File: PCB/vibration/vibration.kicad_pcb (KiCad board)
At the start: 2 copper layers, 45 x 65 mm, 21 parts, among them J1 Conn_01x02, J2 Conn_01x03, J3 Conn_01x03, J4 Conn_01x04, J5 Conn_01x04, Q1 BSS138, Q2 BSS138, U1 NRF24L01_Breakout

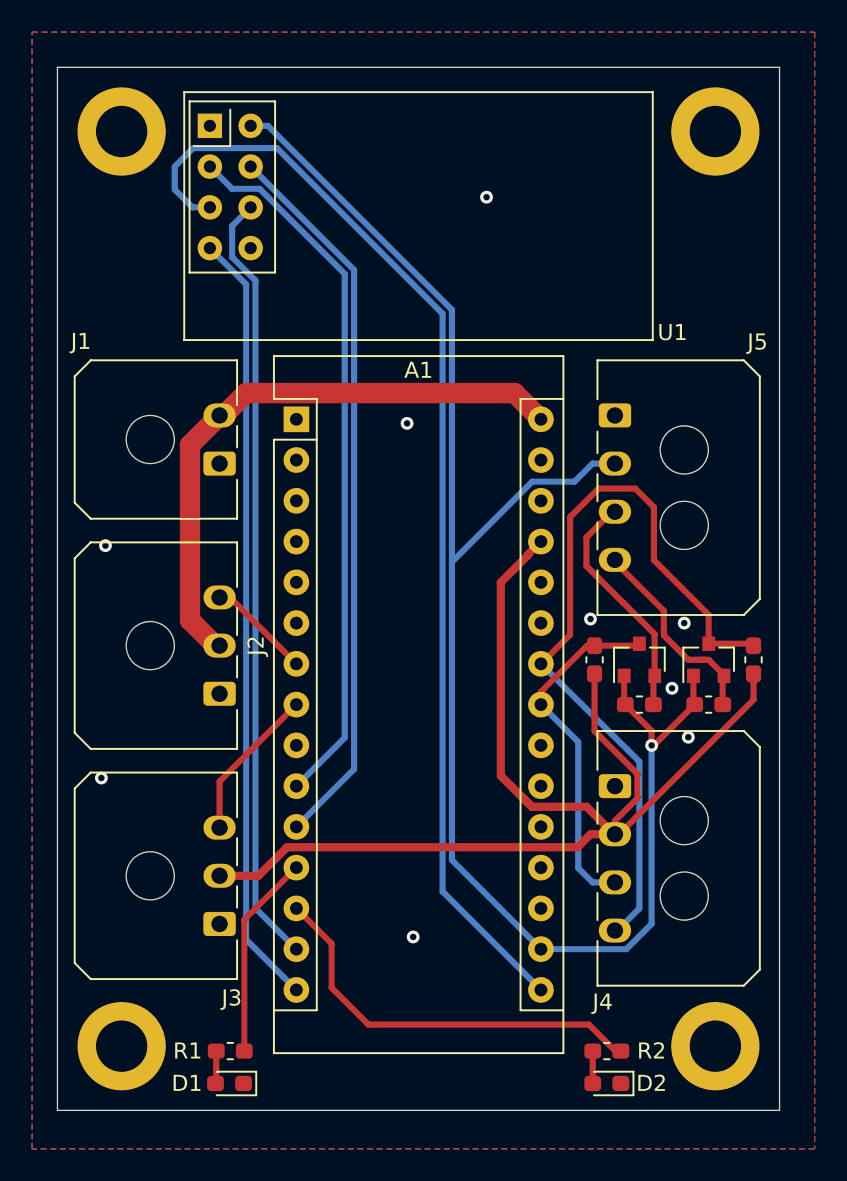
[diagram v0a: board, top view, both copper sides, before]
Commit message: Vibration review complete. Create gerbers
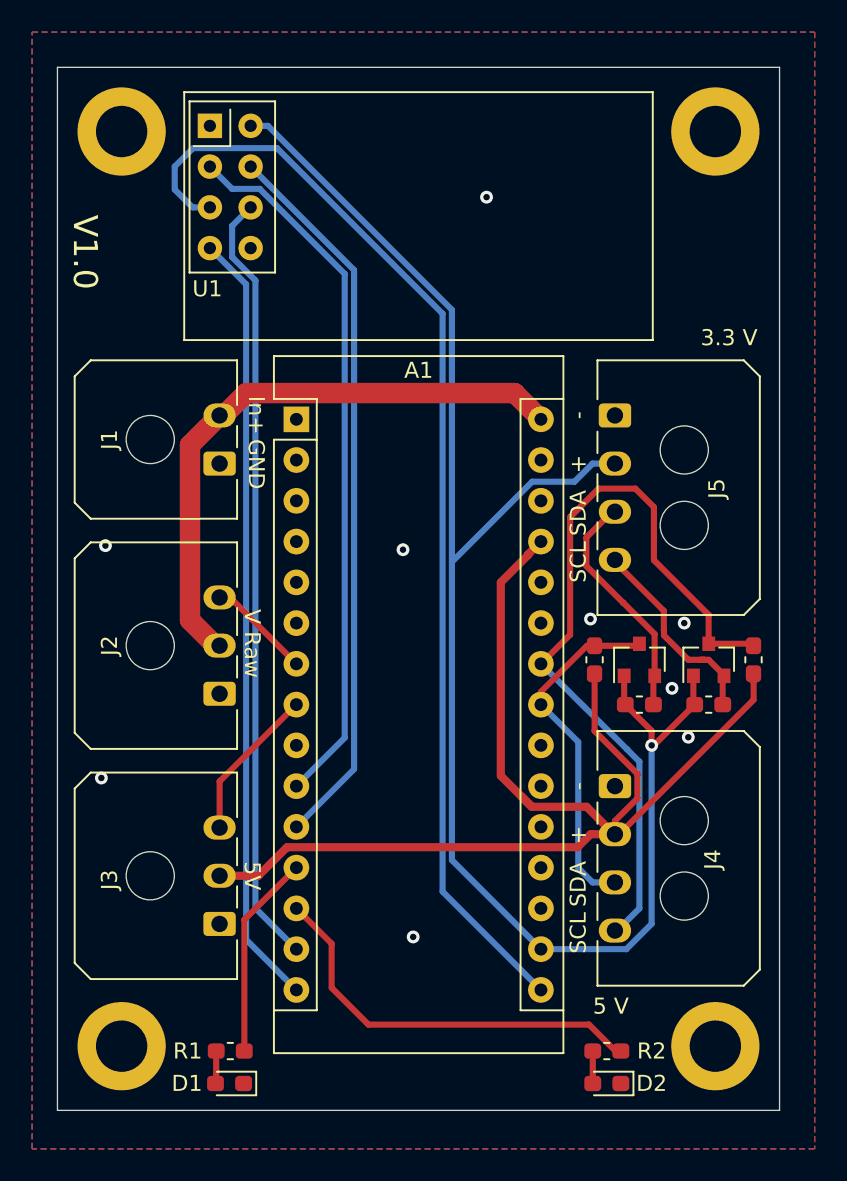
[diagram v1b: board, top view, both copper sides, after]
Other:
- board text added: "+"
- board text added: "-"
- board text added: "3.3 V"
- board text added: "5 V"
- board text added: "5V"
- board text added: "GND"
- board text added: "In+"
- board text added: "SCL"
- board text added: "SDA"
- board text added: "V Raw"
- board text added: "V1.0"
